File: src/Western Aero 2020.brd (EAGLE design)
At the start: 122.2 x 99.4 mm, 85 parts

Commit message: new layout
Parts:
- removed 3.3_TP, 5V_TP, 6V_TP, BAT+_TP, GND_TP, SCA_TP, SCL_TP: PTR1PAD1-13, testpad:P1-13
- removed 7805, 7806: (no value), SparkFun-IC-Power:TO220-IGO
- removed ANALOG, DIGITAL0, DIGITAL2, POWER, SEC_GPS: (no value), SparkFun-Connectors:1X04
- removed AREF, BUZZER, SERIAL: (no value), SparkFun-Connectors:1X02
- removed BAT: (no value), con-phoenix-254:2POL254
- removed D6: Red, SparkFun-LED:LED_3MM
- removed DIGITAL1: (no value), SparkFun-Connectors:1X05
- removed LORA_IO_0, LORA_IO_1, LORA_IO_2, LORA_IO_3, LORA_IO_4, LORA_IO_5: WIREPAD, wirepad:2,15/1,0
- removed PITOT, PI_COMMS: (no value), SparkFun-Connectors:1X03
- removed R26: 10K, SparkFun-Resistors:AXIAL-0.3
- removed SERVO_0, SERVO_1, SERVO_10, SERVO_11, SERVO_12, SERVO_13, SERVO_14, SERVO_15, SERVO_2, SERVO_3, SERVO_4, SERVO_5, SERVO_6, SERVO_7, SERVO_8, SERVO_9: (no value), pinhead:1X03
- removed U$1: TEENSY_3.5_DIL+4, Teensy_3_and_LC_Series_Boards_v1.4:TEENSY_3.5_DIL+4
- removed U$2: SPARKFUN_MPU9250_IMU, AERO_Eagle_Library:SPARKFUN_MPU9250_IMU
- removed U$3: ADAFRUIT_RFM95W_LORA_RADIO, AERO_Eagle_Library:ADAFRUIT_RFM95W_LORA_RADIO
- removed U$4: ADAFRUIT_MPL3115A2_BAROMETER, AERO_Eagle_Library:ADAFRUIT_MPL3115A2_BAROMETER
- removed U$5: ADAFRUIT_INA219_BATTERY_SENSOR, AERO_Eagle_Library:ADAFRUIT_INA219_BATTERY_SENSOR
- removed U$6: ADAFRUIT_MTK3339_GPS, AERO_Eagle_Library:ADAFRUIT_MTK3339_GPS
- added D5: Green, SparkFun-LED:LED_3MM
- added J1, J3: (no value), SparkFun-Connectors:1X03
- added J10, J11, J4, J5, J8: (no value), SparkFun-Connectors:1X04
- added J2, J7, J9: (no value), SparkFun-Connectors:1X02
- added J6: (no value), SparkFun-Connectors:1X05
- added JP1, JP10, JP11, JP12, JP13, JP14, JP15, JP16, JP2, JP3, JP4, JP5, JP6, JP7, JP8, JP9: (no value), pinhead:1X03
- added PAD1, PAD2, PAD3, PAD4, PAD5, PAD6: WIREPAD, wirepad:2,15/1,0
- added R25: 220, SparkFun-Resistors:AXIAL-0.3
- added TP1, TP2, TP3, TP4, TP5, TP6, TP7: PTR1PAD1-13, testpad:P1-13
- added U2: 7805, SparkFun-IC-Power:TO220-IGO
- added U3: TEENSY_3.5_DIL+4, Teensy_3_and_LC_Series_Boards_v1.4:TEENSY_3.5_DIL+4
- added U4: (no value), adafruit:TSSOP28
- added U5: SPARKFUN_MPU9250_IMU, AERO_Eagle_Library:SPARKFUN_MPU9250_IMU
- added U6: ADAFRUIT_MPL3115A2_BAROMETER, AERO_Eagle_Library:ADAFRUIT_MPL3115A2_BAROMETER
- added U7: ADAFRUIT_INA219_BATTERY_SENSOR, AERO_Eagle_Library:ADAFRUIT_INA219_BATTERY_SENSOR
- added U8: ADAFRUIT_RFM95W_LORA_RADIO, AERO_Eagle_Library:ADAFRUIT_RFM95W_LORA_RADIO
- added U9: ADAFRUIT_MTK3339_GPS, AERO_Eagle_Library:ADAFRUIT_MTK3339_GPS
- added X1: (no value), con-phoenix-254:2POL254
- C1: value 10uF -> 0.1uF
- C2: value 0.1uF -> 0.33uF
- C3: value 0.33uF -> 0.1uF
- C4: value 0.1uF -> 10uF
- D1: value Blue -> Red
- D2: value Yellow -> Blue
- D3: value White -> Yellow
- D4: value Green -> White
- R15, R16, R17: value 10K -> 220
- R6, R7, R8, R9: value 220 -> 10K
- U1: value (none) -> 7806; device adafruit:TSSOP28 -> SparkFun-IC-Power:TO220-IGO
- moved R22 105.8 mm to (21.0, 86.5)
- moved R20 95.7 mm to (21.0, 79.5)
- moved R13 80.0 mm to (21.0, 55.0), turned to 180 degrees
- moved U1 73.9 mm to (36.0, 88.5), turned to 90 degrees
- moved D2 73.3 mm to (71.0, 23.5)
- moved D1 71.5 mm to (76.0, 23.5)
- moved C3 69.3 mm to (52.0, 74.8), turned to 90 degrees
- moved D4 67.1 mm to (76.0, 30.5)
- moved D3 63.5 mm to (71.0, 30.5)
- moved R24 63.0 mm to (21.0, 93.5), turned to 180 degrees
- moved R23 54.6 mm to (21.0, 90.0), turned to 180 degrees
- moved SW1 50.6 mm to (72.0, 10.8), turned to 0 degrees
- moved R11 47.6 mm to (21.0, 48.0), turned to 180 degrees
- moved R4 47.0 mm to (62.5, 27.0)
- moved R18 45.0 mm to (21.0, 72.5), turned to 180 degrees
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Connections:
- net 3.3V: now also J11.2, TP7.TP, U3.3.3V, U3.3.3V3, U5.VDD; no longer 3.3_TP.TP, POWER.2, U$1.3.3V, U$1.3.3V3, U$2.VDD
- net 5V: now also C3.1, D5.A, J1.2, J11.1, J4.2, TP6.TP, U2.OUT, U3.VIN, U4.1, U4.2, U4.28, U4.3, U6.VIN, U7.VCC, U8.1, U9.VIN; no longer 5V_TP.TP, 7805.OUT, C1.1, D4.A, PITOT.2, POWER.1, SEC_GPS.2, U$1.VIN, U$3.1, U$4.VIN, U$5.VCC, U$6.VIN, U1.1, U1.2, U1.28, U1.3
- net 6V: now also C1.1, JP1.2, JP10.2, JP11.2, JP12.2, JP13.2, JP14.2, JP15.2, JP16.2, JP2.2, JP3.2, JP4.2, JP5.2, JP6.2, JP7.2, JP8.2, JP9.2, TP1.TP, U1.OUT; no longer 6V_TP.TP, 7806.OUT, C2.1, SERVO_0.2, SERVO_1.2, SERVO_10.2, SERVO_11.2, SERVO_12.2, SERVO_13.2, SERVO_14.2, SERVO_15.2, SERVO_2.2, SERVO_3.2, SERVO_4.2, SERVO_5.2, SERVO_6.2, SERVO_7.2, SERVO_8.2, SERVO_9.2
- net A10: now also J10.1, U3.A10; no longer ANALOG.1, U$1.A10
- net A11: now also J10.2, U3.A11; no longer ANALOG.2, U$1.A11
- net A21: now also J10.3, U3.A21; no longer ANALOG.3, U$1.A21
- net A22: now also J10.4, U3.A22; no longer ANALOG.4, U$1.A22
- net AGND: now also J9.1, U3.AGND; no longer AREF.1, U$1.AGND
- net AREF: now also J9.2, U3.AREF; no longer AREF.2, U$1.AREF
- net BLUE_LED: now also D2.A, U3.21/A7; no longer D1.A, U$1.21/A7
- net BUZZER: now also J2.1, U3.2; no longer BUZZER.1, U$1.2
- net CS: now also J5.4, U3.33/A14, U8.8; no longer DIGITAL2.4, U$1.33/A14, U$3.8
- net D3: now also J8.1, U3.3; no longer DIGITAL0.1, U$1.3
- net D35: now also J6.1, U3.35/A16; no longer DIGITAL1.1, U$1.35/A16
- net D36: now also J6.2, U3.36/A17; no longer DIGITAL1.2, U$1.36/A17
- net D37: now also J6.3, U3.37/A18; no longer DIGITAL1.3, U$1.37/A18
- net D38: now also J6.4, U3.38/A19; no longer DIGITAL1.4, U$1.38/A19
- net D39: now also J6.5, U3.39/A20; no longer DIGITAL1.5, U$1.39/A20
- net D4: now also J8.2, U3.4; no longer DIGITAL0.2, U$1.4
- net D5: now also J8.3, U3.5; no longer DIGITAL0.3, U$1.5
- net D6: now also J8.4, U3.6; no longer DIGITAL0.4, U$1.6
- net DIP1: now also R6.P$2, U3.24; no longer R26.P$2, U$1.24
- net DIP2: now also R7.P$2, U3.25; no longer R15.P$2, U$1.25
- net DIP3: now also R8.P$2, U3.26; no longer R16.P$2, U$1.26
- net DIP4: now also R9.P$2, U3.27; no longer R17.P$2, U$1.27
- net ENV_INT1: now also U3.29, U6.INT1; no longer U$1.29, U$4.INT1
- net ENV_INT2: now also U3.30, U6.INT2; no longer U$1.30, U$4.INT2
- net GND: now also J1.1, J11.4, J2.2, J3.1, J4.1, JP1.3, JP10.3, JP11.3, JP12.3, JP13.3, JP14.3, JP15.3, JP16.3, JP2.3, JP3.3, JP4.3, JP5.3, JP6.3, JP7.3, JP8.3, JP9.3, R1.P$1, R2.P$1, R3.P$1, R4.P$1, R5.P$1, R6.P$1, R7.P$1, R8.P$1, R9.P$1, TP2.TP, U1.GND, U2.GND, U3.GND, U3.GND1, U4.14, U4.23, U4.24, U4.25, U4.4, U4.5, U5.AD0, U5.FSYNC, U5.GND, U6.GND, U7.GND, U8.2, U9.GND, X1.1; no longer 7805.GND, 7806.GND, BAT.1, BUZZER.2, GND_TP.TP, PITOT.1, PI_COMMS.1, POWER.4, R10.P$1, R11.P$1, R12.P$1, R13.P$1, R14.P$1, R15.P$1, R16.P$1, R17.P$1, R26.P$1, SEC_GPS.1, SERVO_0.3, SERVO_1.3, SERVO_10.3, SERVO_11.3, SERVO_12.3, SERVO_13.3, SERVO_14.3, SERVO_15.3, SERVO_2.3, SERVO_3.3, SERVO_4.3, SERVO_5.3, SERVO_6.3, SERVO_7.3, SERVO_8.3, SERVO_9.3, U$1.GND, U$1.GND1, U$2.AD0, U$2.FSYNC, U$2.GND, U$3.2, U$4.GND, U$5.GND, U$6.GND, U1.14, U1.23, U1.24, U1.25, U1.4, U1.5
- net GPS_EN: now also U3.15/A1, U9.EN; no longer U$1.15/A1, U$6.EN
- net GPS_FIX: now also U3.16/A2, U9.FIX; no longer U$1.16/A2, U$6.FIX
- net GPS_PPS: now also U3.17/A3, U9.PPS; no longer U$1.17/A3, U$6.PPS
- net IMU_INT: now also U3.28, U5.INT; no longer U$1.28, U$2.INT
- net LORA_EN: now also U3.32/A13, U8.3; no longer U$1.32/A13, U$3.3
- net LORA_INT: now also U3.31/A12; no longer U$1.31/A12
- net LORA_RST: now also U3.34/A15, U8.9; no longer U$1.34/A15, U$3.9
- net MISO: now also J5.2, U3.12, U8.6; no longer DIGITAL2.2, U$1.12, U$3.6
- net MOSI: now also J5.3, U3.11, U8.7; no longer DIGITAL2.3, U$1.11, U$3.7
- net N$1: now also JP1.1, R10.P$2; no longer R18.P$2, SERVO_0.1
- net N$10: now also PAD3.1, U8.11; no longer LORA_IO_2.1, U$3.11
- net N$11: now also JP3.1, R12.P$2; no longer R2.P$2, SERVO_2.1
- net N$12: now also JP4.1, R13.P$2; no longer R3.P$2, SERVO_3.1
- net N$13: now also JP5.1, R14.P$2; no longer R4.P$2, SERVO_4.1
- net N$14: now also JP6.1, R15.P$2; no longer R5.P$2, SERVO_5.1
- net N$15: now also JP7.1, R16.P$2; no longer R6.P$2, SERVO_6.1
- net N$16: now also JP8.1, R17.P$2; no longer R7.P$2, SERVO_7.1
- net N$17: now also JP9.1, R18.P$2; no longer R8.P$2, SERVO_8.1
- net N$18: now also JP10.1, R19.P$2; no longer R9.P$2, SERVO_9.1
- net N$19: now also JP11.1, R20.P$2; no longer R19.P$2, SERVO_10.1
- net N$2: now also D1.K, R1.P$2; no longer D6.K, R10.P$2
- net N$20: now also JP12.1, R21.P$2; no longer R20.P$2, SERVO_11.1
- net N$21: now also JP13.1, R22.P$2; no longer R21.P$2, SERVO_12.1
- net N$22: now also JP14.1, R23.P$2; no longer R22.P$2, SERVO_13.1
- net N$23: now also JP15.1, R24.P$2; no longer R23.P$2, SERVO_14.1
- net N$24: now also JP16.1, R25.P$2; no longer R24.P$2, SERVO_15.1
- net N$25: now also PAD5.1, U8.13; no longer LORA_IO_4.1, U$3.13
- net N$26: now also PAD4.1, U8.12; no longer LORA_IO_3.1, U$3.12
- net N$27: now also PAD1.1, U8.4; no longer LORA_IO_0.1, U$3.4
- net N$3: now also D2.K, R2.P$2; no longer D1.K, R11.P$2
- net N$4: now also D3.K, R3.P$2; no longer D2.K, R12.P$2
- net N$5: now also D4.K, R5.P$2; no longer D3.K, R13.P$2
- net N$6: now also D5.K, R4.P$2; no longer D4.K, R14.P$2
- net N$7: now also PAD6.1, U8.14; no longer LORA_IO_5.1, U$3.14
- net N$8: now also PAD2.1, U8.10; no longer LORA_IO_1.1, U$3.10
- net N$9: now also JP2.1, R11.P$2; no longer R1.P$2, SERVO_1.1
- net PITOT: now also J1.3, U3.14/A0; no longer PITOT.3, U$1.14/A0
- net PWM0: now also R10.P$1, U4.6; no longer R18.P$1, U1.6
- net PWM1: now also R11.P$1, U4.7; no longer R1.P$1, U1.7
- net PWM10: now also R20.P$1, U4.17; no longer R19.P$1, U1.17
- net PWM11: now also R21.P$1, U4.18; no longer R20.P$1, U1.18
- net PWM12: now also R22.P$1, U4.19; no longer R21.P$1, U1.19
- net PWM13: now also R23.P$1, U4.20; no longer R22.P$1, U1.20
- net PWM14: now also R24.P$1, U4.21; no longer R23.P$1, U1.21
- net PWM15: now also R25.P$1, U4.22; no longer R24.P$1, U1.22
- net PWM2: now also R12.P$1, U4.8; no longer R2.P$1, U1.8
- net PWM3: now also R13.P$1, U4.9; no longer R3.P$1, U1.9
- net PWM4: now also R14.P$1, U4.10; no longer R4.P$1, U1.10
- net PWM5: now also R15.P$1, U4.11; no longer R5.P$1, U1.11
- net PWM6: now also R16.P$1, U4.12; no longer R6.P$1, U1.12
- net PWM7: now also R17.P$1, U4.13; no longer R7.P$1, U1.13
- net PWM8: now also R18.P$1, U4.15; no longer R8.P$1, U1.15
- net PWM9: now also R19.P$1, U4.16; no longer R9.P$1, U1.16
- net RED_LED: now also D1.A, U3.20/A6; no longer D6.A, U$1.20/A6
- net RX1: now also J7.1, U3.0; no longer SERIAL.1, U$1.0
- net RX2: now also J3.3, U3.9; no longer PI_COMMS.3, U$1.9
- net RX3: now also J4.4, U3.7, U9.RX; no longer SEC_GPS.4, U$1.7, U$6.RX
- net SCK: now also J5.1, U3.13, U8.5; no longer DIGITAL2.1, U$1.13, U$3.5
- net SCL: now also TP3.TP, U3.19/A5, U4.26, U5.SCL, U6.SCL, U7.SCL; no longer SCL_TP.TP, U$1.19/A5, U$2.SCL, U$4.SCL, U$5.SCL, U1.26
- net SDA: now also TP5.TP, U3.18/A4, U4.27, U5.SDA, U6.SDA, U7.SDA; no longer SCA_TP.TP, U$1.18/A4, U$2.SDA, U$4.SDA, U$5.SDA, U1.27
- net TX1: now also J7.2, U3.1; no longer SERIAL.2, U$1.1
- net TX2: now also J3.2, U3.10; no longer PI_COMMS.2, U$1.10
- net TX3: now also J4.3, U3.8, U9.TX; no longer SEC_GPS.3, U$1.8, U$6.TX
- net VIN+: now also TP4.TP, U7.VIN+, X1.2; no longer BAT+_TP.TP, BAT.2, U$5.VIN+
- net VIN-: now also C2.1, U1.IN, U2.IN, U7.VIN-; no longer 7805.IN, 7806.IN, C3.1, U$5.VIN-
- net VUSB: now also J11.3, U3.VUSB; no longer POWER.3, U$1.VUSB
- net WHITE_LED: now also D4.A, U3.23/A9; no longer D3.A, U$1.23/A9
- net YELLOW_LED: now also D3.A, U3.22/A8; no longer D2.A, U$1.22/A8
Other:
- board size 122.2 x 99.4 mm -> 126.2 x 101.9 mm
- board text added: "Jeff St. Jean"
- board text added: "Western Engineering Aero Design 2019/2020"
- board text removed: "Western Engineering Aero Design"

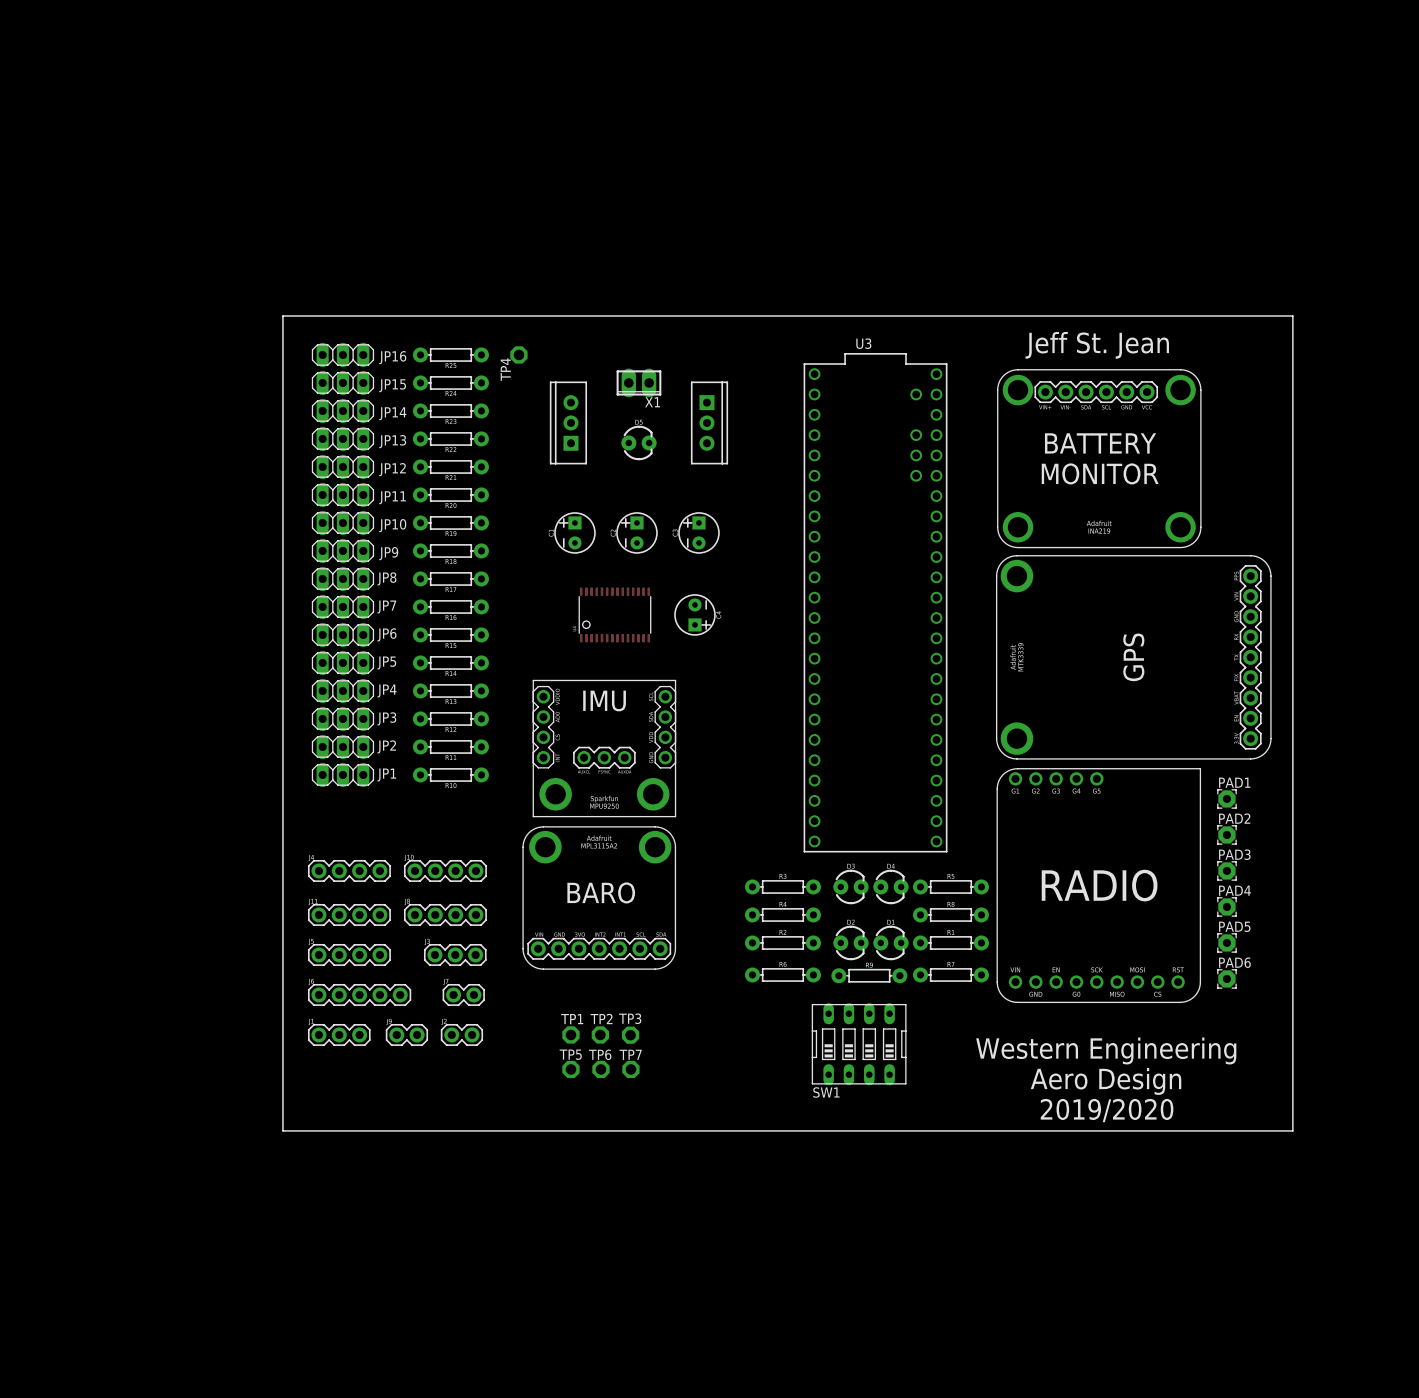
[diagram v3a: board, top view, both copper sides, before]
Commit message: Add new voltage regulator
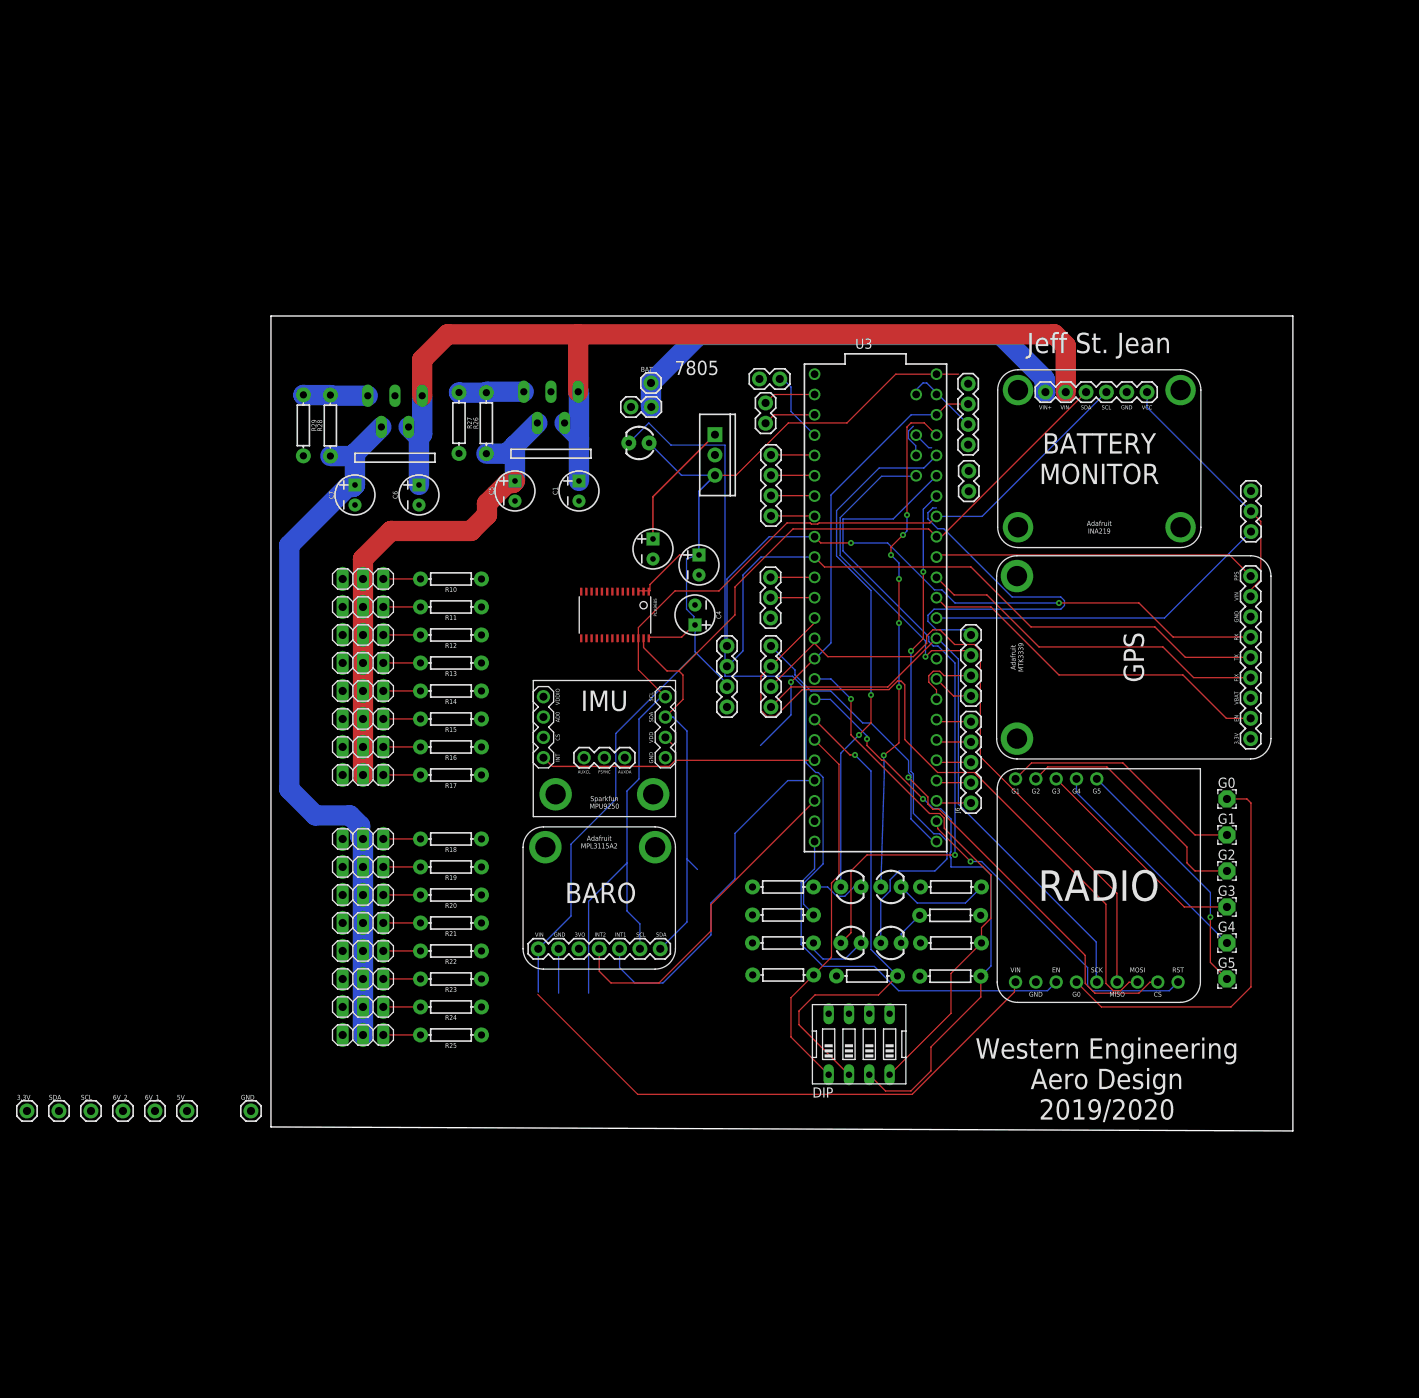
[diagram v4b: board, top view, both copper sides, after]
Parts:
- removed TP1, TP2, TP3, TP4, TP5, TP6, TP7: PTR1PAD1-13, testpad:P1-13
- removed U1: 7806, SparkFun-IC-Power:TO220-IGO
- removed U2: 7805, SparkFun-IC-Power:TO220-IGO
- removed X1: (no value), con-phoenix-254:2POL254
- added 3.3V, 5V, 6V_1, 6V_2, BAT, GND, SCL, SDA: (no value), SparkFun-Connectors:1X01
- added 7805: 7805, SparkFun-IC-Power:TO220-IGO
- added C5, C7: 22uF, SparkFun-Capacitors:CPOL-RADIAL-2.5MM-5MM
- added C6: 10uF, SparkFun-Capacitors:CPOL-RADIAL-2.5MM-5MM
- added IC1, IC2: LT1963AET, linear-technology:TO220-5
- added J12: POWER, SparkFun-Connectors:1X02
- added R26, R28: 3800, SparkFun-Resistors:AXIAL-0.3
- added R27, R29: 1000, SparkFun-Resistors:AXIAL-0.3
- C1: value 0.1uF -> 10uF
- J1: value (none) -> PITOT
- J10: value (none) -> ANA_IO
- J11: value (none) -> PWR
- J2: value (none) -> BUZZER
- J3: value (none) -> RX2/TX2
- J4: value (none) -> RX3/TX3
- J5: value (none) -> SPI
- J6, J8: value (none) -> DIG_IO
- J7: value (none) -> RX1/TX1
- J9: value (none) -> REF/GND
- JP1: value (none) -> PWM0
- JP10: value (none) -> PWM9
- JP11: value (none) -> PWM10
- JP12: value (none) -> PWM11
- JP13: value (none) -> PWM12
- JP14: value (none) -> PWM13
- JP15: value (none) -> PWM14
- JP16: value (none) -> PWM15
- JP2: value (none) -> PWM1
- JP3: value (none) -> PWM2
- JP4: value (none) -> PWM3
- JP5: value (none) -> PWM4
- JP6: value (none) -> PWM5
- JP7: value (none) -> PWM6
- JP8: value (none) -> PWM7
- JP9: value (none) -> PWM8
- moved J1 134.9 mm to (121.0, 80.0), turned to 270 degrees
- moved J11 104.9 mm to (85.7, 93.4), turned to 270 degrees
- moved J9 100.4 mm to (85.7, 82.5), turned to 270 degrees
- moved J2 91.7 mm to (62.1, 94.0), turned to 180 degrees
- moved JP16 85.0 mm to (10.0, 12.0), turned to 180 degrees
- moved R25 85.0 mm to (21.0, 12.0)
- moved J6 85.0 mm to (86.0, 41.0), turned to 90 degrees
- moved J7 83.6 mm to (60.3, 91.0), turned to 270 degrees
- moved JP15 78.0 mm to (10.0, 15.5), turned to 180 degrees
- moved R24 78.0 mm to (21.0, 15.5)
- moved J10 75.5 mm to (86.0, 62.0), turned to 270 degrees
- moved J8 72.7 mm to (61.0, 84.5), turned to 270 degrees
- moved JP14 71.0 mm to (10.0, 19.0), turned to 180 degrees
- moved R23 71.0 mm to (21.0, 19.0)
- moved J5 64.4 mm to (61.0, 53.0), turned to 90 degrees
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- renumbered PAD1 to G0, PAD2 to G1, PAD3 to G2, PAD4 to G3, PAD5 to G4, PAD6 to G5, SW1 to DIP, U4 to PCA9685
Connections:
- removed net 6V: C1.1, JP1.2, JP10.2, JP11.2, JP12.2, JP13.2, JP14.2, JP15.2, JP16.2, JP2.2, JP3.2, JP4.2, JP5.2, JP6.2, JP7.2, JP8.2, JP9.2, TP1.TP, U1.OUT
- new net 6V_1: 6V_1.1, C5.1, IC2.4, JP1.2, JP2.2, JP3.2, JP4.2, JP5.2, JP6.2, JP7.2, JP8.2, R26.P$1
- new net 6V_2: 6V_2.1, C7.1, IC1.4, JP10.2, JP11.2, JP12.2, JP13.2, JP14.2, JP15.2, JP16.2, JP9.2, R28.P$1
- new net N$28: IC1.5, R28.P$2, R29.P$1
- new net N$29: IC2.5, R26.P$2, R27.P$1
- net 3.3V: now also 3.3V.1; no longer TP7.TP
- net 5V: now also 5V.1, 7805.OUT; no longer TP6.TP, U2.OUT
- net GND: now also 7805.GND, C5.2, C6.2, C7.2, GND.1, IC1.3, IC2.3, J12.1, R27.P$2, R29.P$2; no longer TP2.TP, U1.GND, U2.GND, X1.1
- net SCL: now also SCL.1; no longer TP3.TP
- net SDA: now also SDA.1; no longer TP5.TP
- net VIN+: now also BAT.1, J12.2; no longer TP4.TP, X1.2
- net VIN-: now also 7805.IN, C1.1, C6.1, IC1.1, IC1.2, IC2.1, IC2.2; no longer U1.IN, U2.IN
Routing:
- net 5V: track 0.00 -> 246.6 mm
- net VIN-: track 0.00 -> 143.0 mm
- net SCL: track 0.00 -> 133.6 mm
- net SDA: track 0.00 -> 115.7 mm
- net 6V_2: track 0.00 -> 90.7 mm
- net MOSI: track 0.00 -> 89.8 mm
- net BLUE_LED: track 0.00 -> 85.4 mm, vias 0 -> 1
- net N$6: track 0.00 -> 84.7 mm
- net TX3: track 0.00 -> 81.9 mm
- net MISO: track 0.00 -> 81.8 mm
- net RX3: track 0.00 -> 81.2 mm, vias 0 -> 2
- net CS: track 0.00 -> 81.1 mm, vias 0 -> 1
- net SCK: track 0.00 -> 75.6 mm
- net DIP2: track 0.00 -> 72.6 mm, vias 0 -> 2
- net DIP1: track 0.00 -> 65.8 mm, vias 0 -> 1
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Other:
- board size 126.2 x 101.9 mm -> 127.7 x 101.9 mm
- board text added: "7805"
